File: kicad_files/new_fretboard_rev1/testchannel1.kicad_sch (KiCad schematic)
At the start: 22 parts, among them U3 LX3302AQPW-TR-EASY

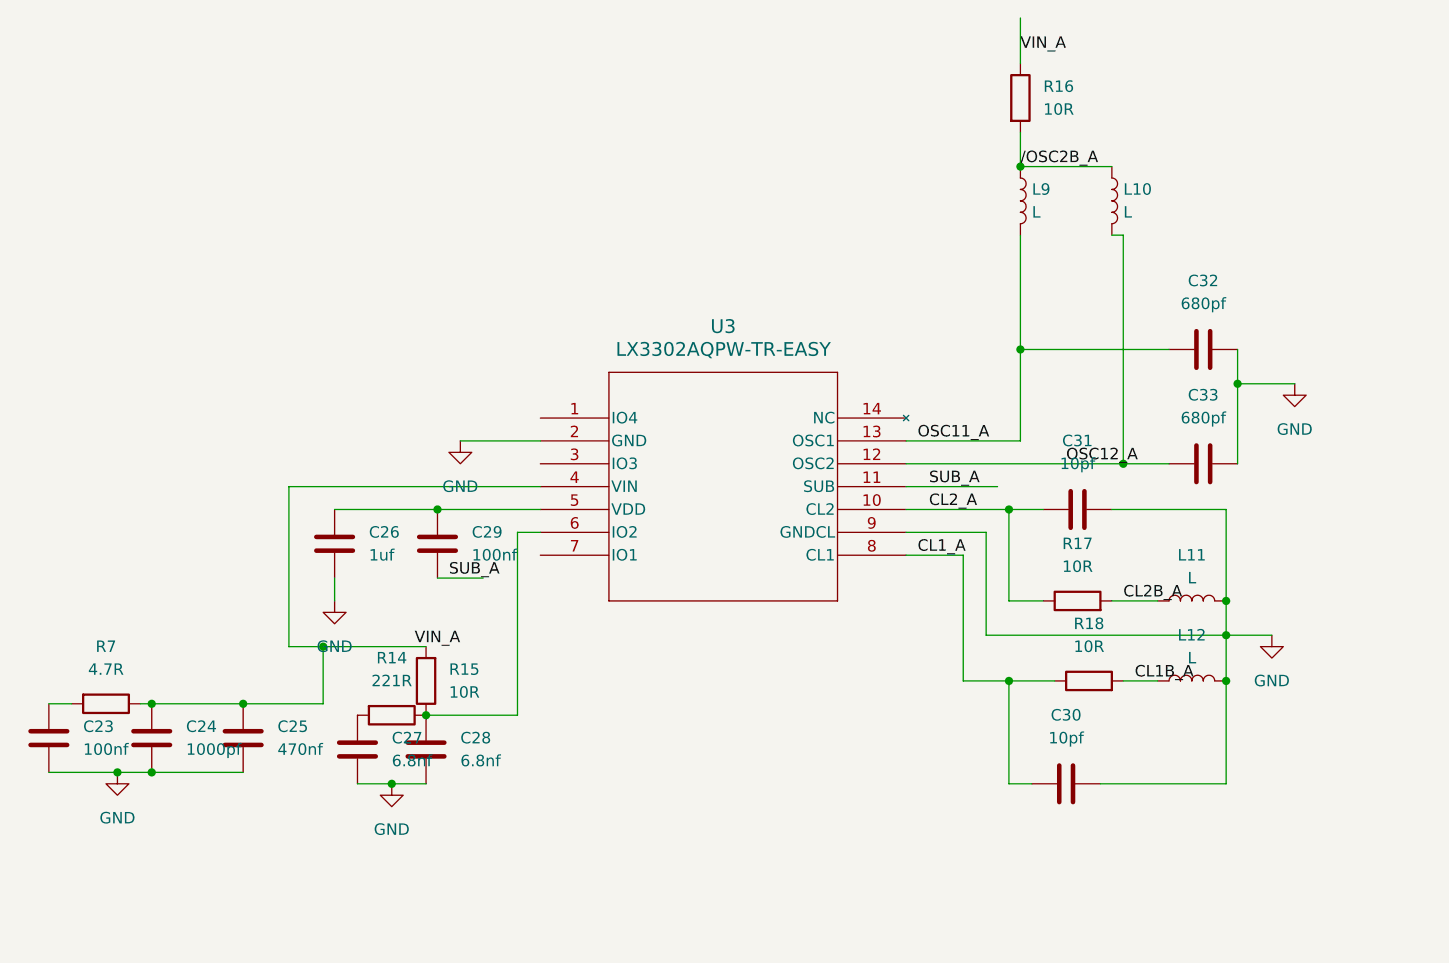
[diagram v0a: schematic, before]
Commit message: stm32 micro added
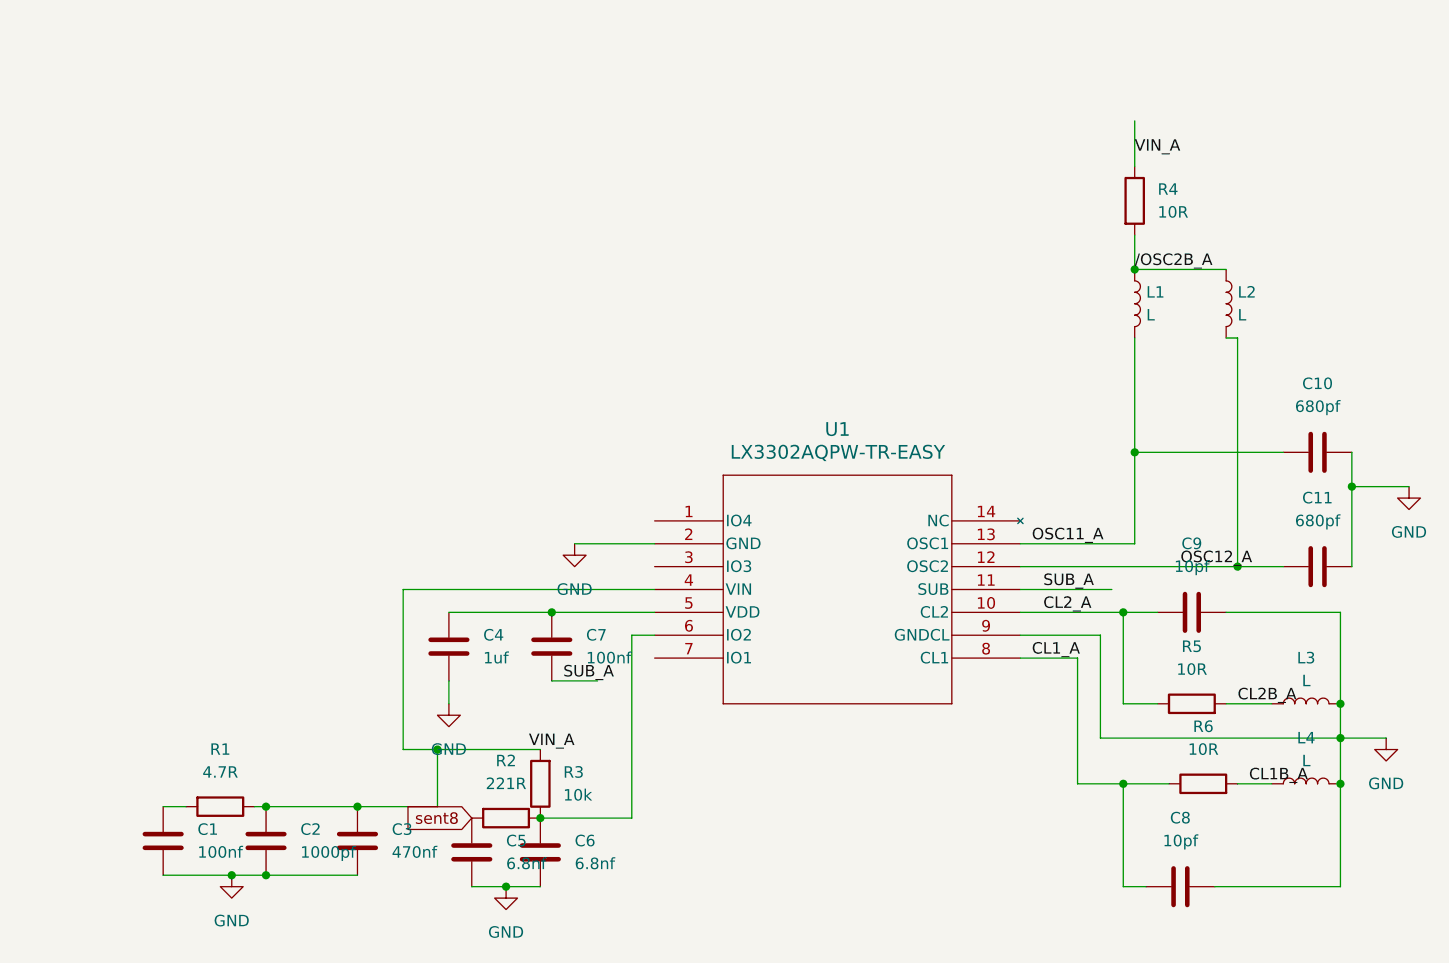
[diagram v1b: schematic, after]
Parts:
- removed C23, C29: 100nf, Capacitor_SMD:C_0402_1005Metric, symbol Device:C
- removed C24: 1000pf, Capacitor_SMD:C_0402_1005Metric, symbol Device:C
- removed C25: 470nf, Capacitor_SMD:C_0402_1005Metric, symbol Device:C
- removed C26: 1uf, Capacitor_SMD:C_0603_1608Metric, symbol Device:C
- removed C27, C28: 6.8nf, Capacitor_SMD:C_0402_1005Metric, symbol Device:C
- removed C30, C31: 10pf, Capacitor_SMD:C_0402_1005Metric, symbol Device:C
- removed C32, C33: 680pf, Capacitor_SMD:C_0603_1608Metric, symbol Device:C
- removed L10, L11, L12, L9: L, NetTie:NetTie-2_SMD_Pad0.5mm, symbol Device:L
- removed R14: 221R, Resistor_SMD:R_0402_1005Metric, symbol Device:R
- removed R15, R16, R17, R18: 10R, Resistor_SMD:R_0402_1005Metric, symbol Device:R
- removed R7: 4.7R, Resistor_SMD:R_0402_1005Metric, symbol Device:R
- removed U3: LX3302AQPW-TR-EASY, Snapeda:14-TSSOP_MCH-L, symbol Snapeda:LX3302AQPW-TR-EASY
- added C1, C7: 100nf, Capacitor_SMD:C_0402_1005Metric, symbol Device:C
- added C10, C11: 680pf, Capacitor_SMD:C_0603_1608Metric, symbol Device:C
- added C2: 1000pf, Capacitor_SMD:C_0402_1005Metric, symbol Device:C
- added C3: 470nf, Capacitor_SMD:C_0402_1005Metric, symbol Device:C
- added C4: 1uf, Capacitor_SMD:C_0603_1608Metric, symbol Device:C
- added C5, C6: 6.8nf, Capacitor_SMD:C_0402_1005Metric, symbol Device:C
- added C8, C9: 10pf, Capacitor_SMD:C_0402_1005Metric, symbol Device:C
- added L1, L2, L3, L4: L, NetTie:NetTie-2_SMD_Pad0.5mm, symbol Device:L
- added R1: 4.7R, Resistor_SMD:R_0402_1005Metric, symbol Device:R
- added R2: 221R, Resistor_SMD:R_0402_1005Metric, symbol Device:R
- added R3: 10k, Resistor_SMD:R_0402_1005Metric, symbol Device:R
- added R4, R5, R6: 10R, Resistor_SMD:R_0402_1005Metric, symbol Device:R
- added U1: LX3302AQPW-TR-EASY, Snapeda:14-TSSOP_MCH-L, symbol Snapeda:LX3302AQPW-TR-EASY
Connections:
- net /OSC2B_A: now also L1.1, L2.1, R4.2
- net CL1B_A: now also L4.1, R6.2
- net CL1_A: now also C8.1, R6.1, U1.8 (CL1)
- net CL2B_A: now also L3.1, R5.2
- net CL2_A: now also C9.1, R5.1, U1.10 (CL2)
- net GND: now also C1.1, C10.2, C11.2, C2.1, C3.1, C4.1, C5.1, C6.1, C8.2, C9.2, L3.2, L4.2, U1.2 (GND), U1.9 (GNDCL)
- net OSC11_A: now also C10.1, L1.2, U1.13 (OSC1)
- net OSC12_A: now also C11.1, L2.2, U1.12 (OSC2)
- net SUB_A: now also C7.1, U1.11 (SUB)
- net VIN_A: now also C2.2, C3.2, R1.1, R3.2, R4.1, U1.4 (VIN)
- new net: C4.2, C7.2, U1.5 (VDD)
- new net: C6.2, R2.1, R3.1, U1.6 (IO2)
- new net: C1.2, R1.2
- new net sent8: C5.2, R2.2

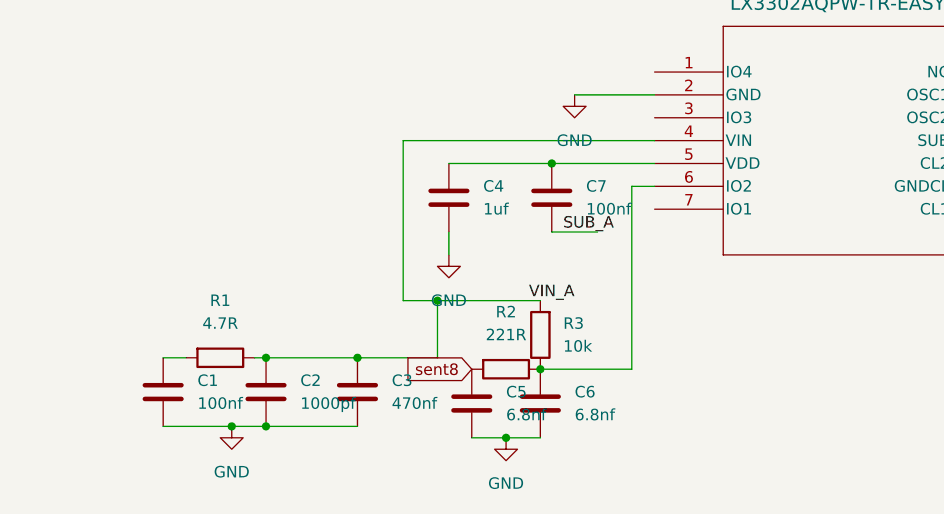
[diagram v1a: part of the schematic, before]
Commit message: mcu configured, still needs power connections and spi i2c connections
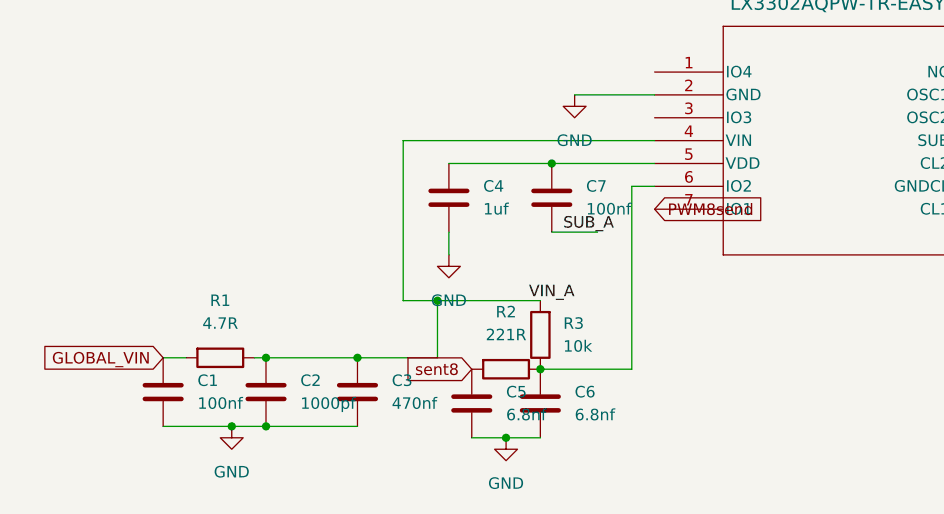
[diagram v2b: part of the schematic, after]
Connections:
- net PWM8send: now reaches U1.7 (IO1)
- net GLOBAL_VIN: now reaches C1.2, R1.2
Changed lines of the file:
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@@
+		)
+	)
+	(global_label "GLOBAL_VIN"
+		(shape input)
+		(at 55.88 130.81 180)
+		(fields_autoplaced yes)
+		(effects
+			(font
+				(size 1.27 1.27)
+			)
+			(justify right)
+		)
+		(property "Intersheetrefs" "${INTERSHEET_REFS}"
+			(at 41.888 130.81 0)
+			(effects
+				(font
+					(size 1.27 1.27)
+				)
+				(justify right)
+				(hide yes)
+			)
+		)
+	)
+	(global_label "PWM8send"
+		(shape input)
+		(at 110.49 114.3 0)
+		(fields_autoplaced yes)
+		(effects
+			(font
+				(size 1.27 1.27)
+			)
+			(justify left)
+		)
+		(property "Intersheetrefs" "${INTERSHEET_REFS}"
+			(at 123.2722 114.3 0)
+			(effects
+				(font
+					(size 1.27 1.27)
+				)
+				(justify left)
+				(hide yes)
+			)
 		)
 	)

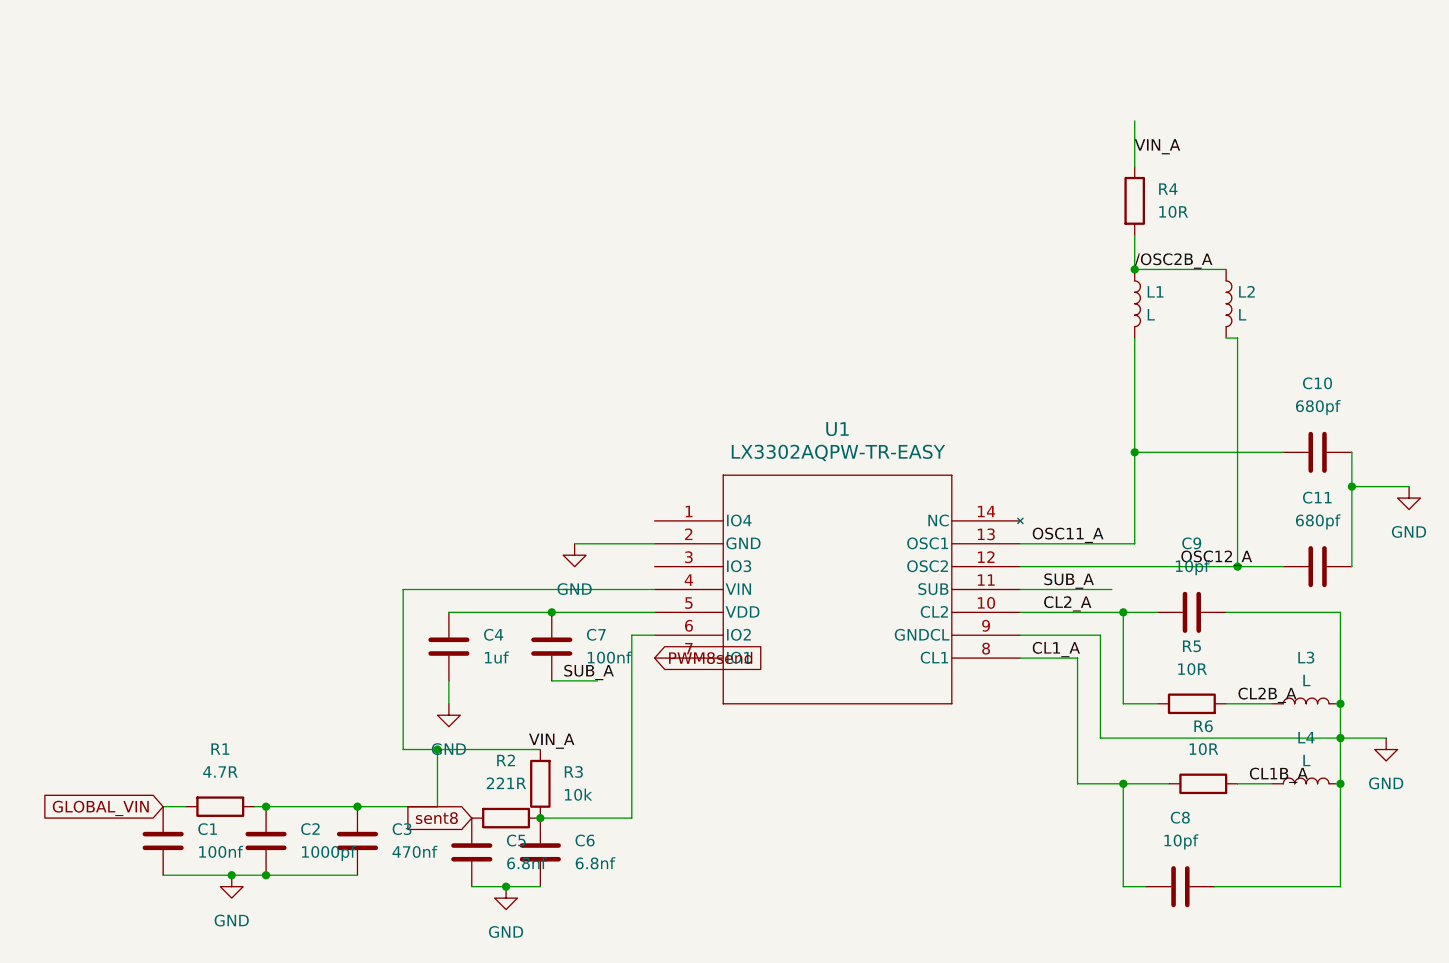
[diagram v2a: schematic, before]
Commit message: finished routing - adding silkscreen
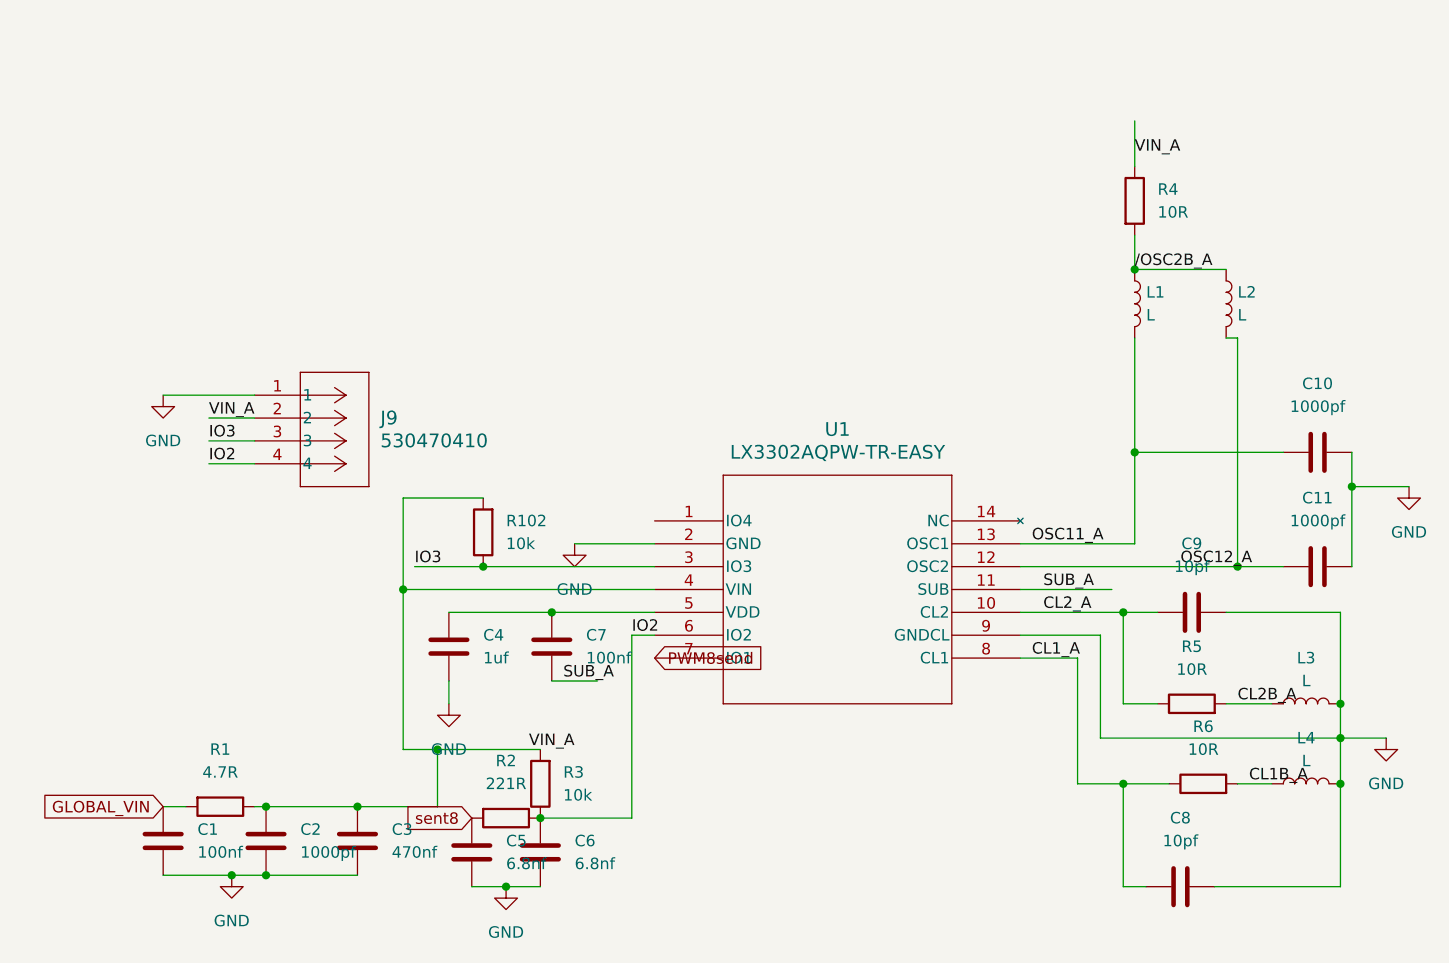
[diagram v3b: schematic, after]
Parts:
- added J9: 530470410, Snapeda:CONN04_530470410_MOL, symbol Snapeda:530470410
- added R102: 10k, Resistor_SMD:R_0402_1005Metric, symbol Device:R
- C10, C11: value 680pf -> 1000pf
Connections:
- net GND: now also J9.1
- net VIN_A: now also J9.2, R102.2
- net IO3: now reaches U1.3 (IO3)
- net IO3: now also J9.3, R102.1
- net IO2: now reaches C6.2, R2.1, R3.1, U1.6 (IO2)
- net IO2: now also J9.4

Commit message: exported gerbers of lefthand
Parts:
- L1, L2, L3, L4: now left out of the parts list
